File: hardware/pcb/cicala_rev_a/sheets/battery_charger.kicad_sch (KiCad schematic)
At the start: 34 parts, among them J1 USB-C receptacle, J3 Protected LiPo + NTC, U2 BQ25185DLH, U3 TPS63802DLA, U4 USBLC6-2SC6, U5 TPS22917DBVR

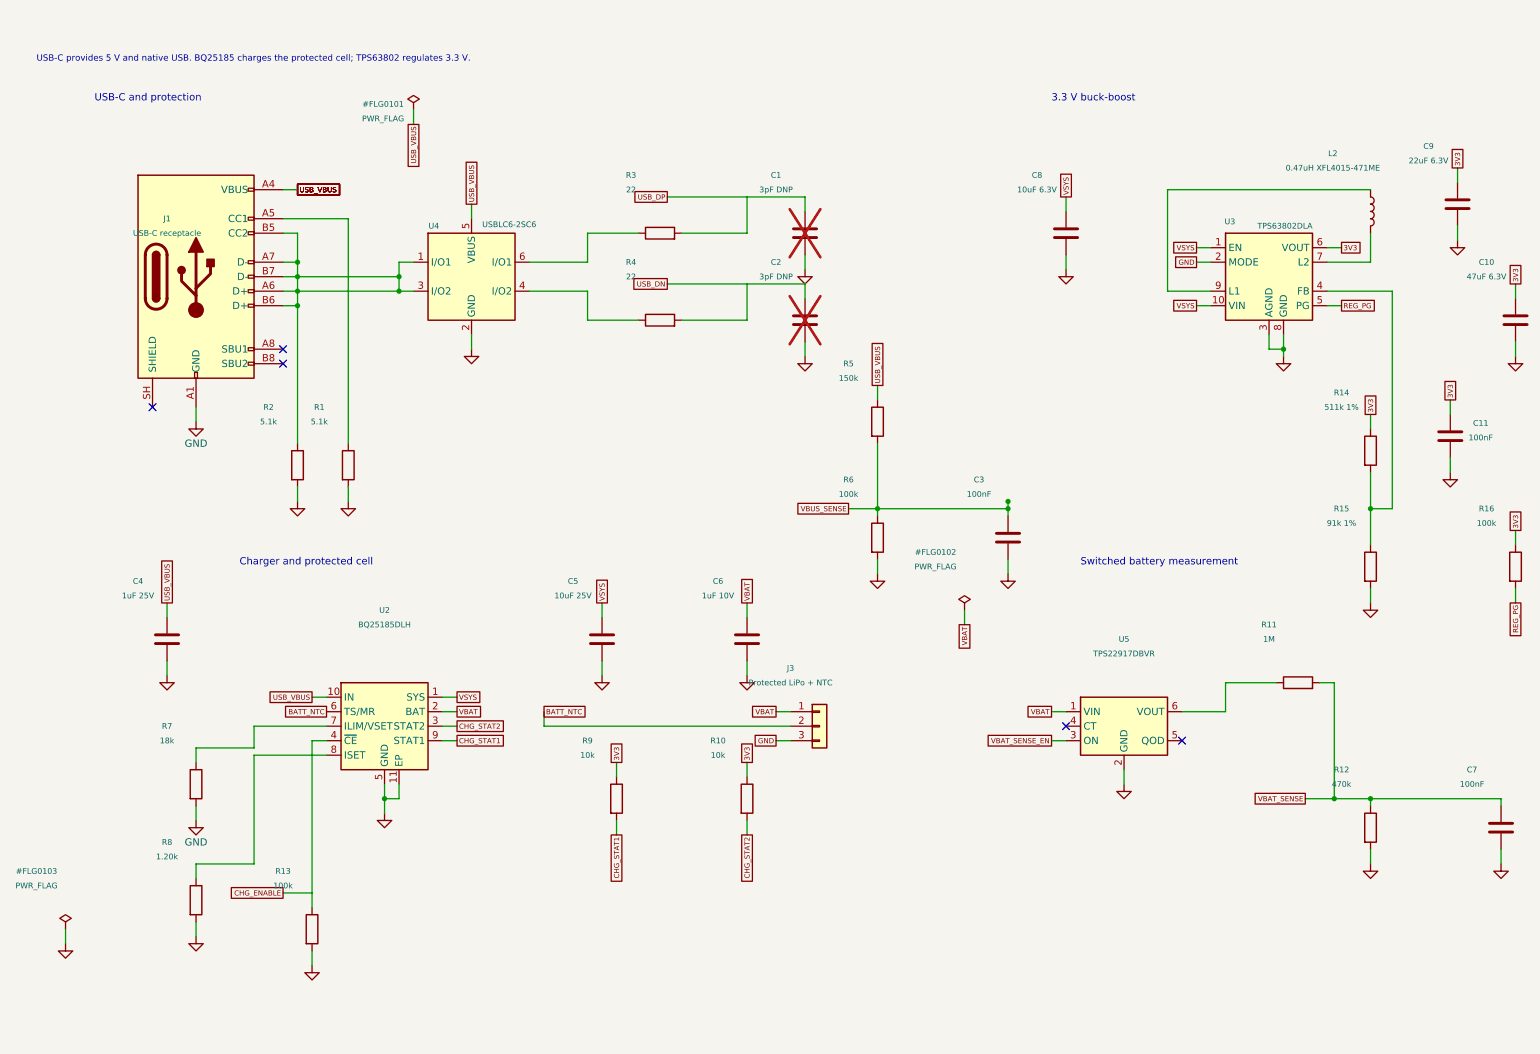
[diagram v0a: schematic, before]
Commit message: fix(hw): split the shorted USB pair and PREVGL pump node
Sheet re-layout that also separates two nets that were tied together.

J1 CC2, D+ and D- shared one net with both USBLC6 line pins; D+ and D-
are now their own nets. D1 had both pins on EPD_PREVGL, shorting it out
of the charge pump; its cathode is now the pump node with C16.

Three net labels were lost in the move and are now auto-named:
BATT_NTC, BTN_CATEGORY and BTN_NEXT. pin_contract.csv and BOM.md still
name them, so they need restoring.

Co-Authored-By: Claude Opus 5 (1M context) <noreply@anthropic.com>
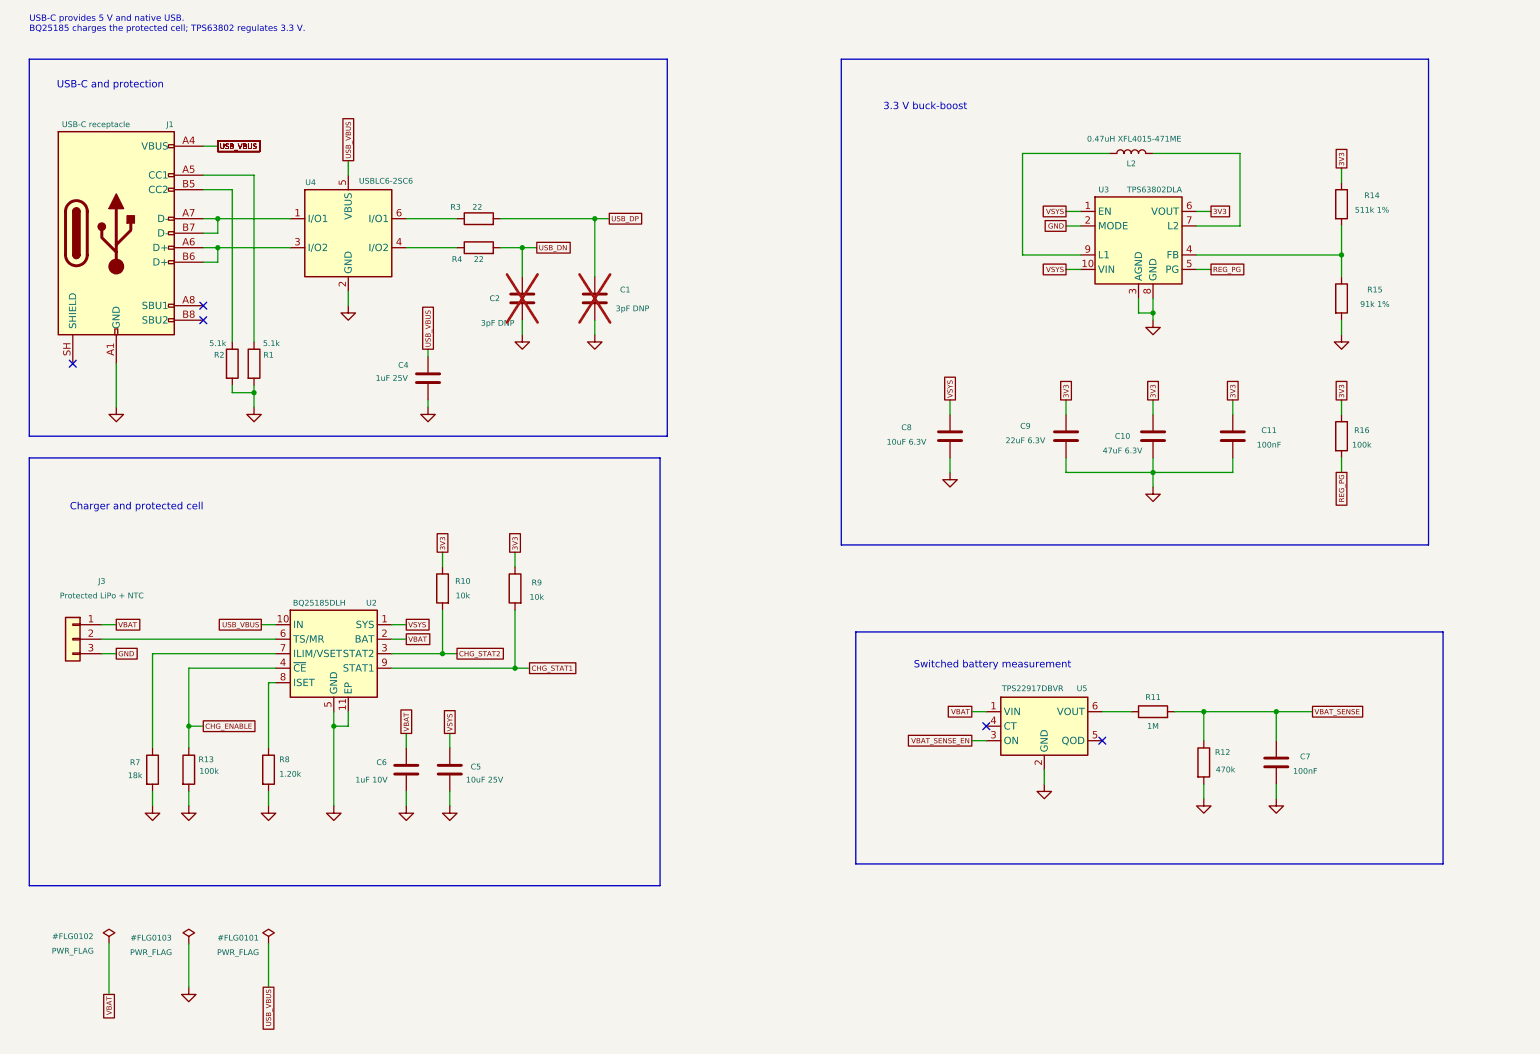
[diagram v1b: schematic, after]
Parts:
- removed C3: 100nF, Capacitor_SMD:C_0603_1608Metric, symbol Device:C
- removed R5: 150k, Resistor_SMD:R_0603_1608Metric, symbol Device:R
- removed R6: 100k, Resistor_SMD:R_0603_1608Metric, symbol Device:R
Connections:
- net BATT_NTC: no longer names the net of J3.2 (Pin_2), U2.6 (TS/MR)
- new net: J1.A6 (D+), J1.B6 (D+), U4.3 (I/O2)
- new net: J1.A7 (D-), J1.B7 (D-), U4.1 (I/O1)
- new net: J1.B5 (CC2), R2.1
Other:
- moved on the sheet: C1, C10, C11, C2, C4, C5, C6, C7, C8, C9, J1, J3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

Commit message: fix(hw): correct four ERC-invisible rev A wiring errors
All four are electrically valid connections that are simply wrong, which
is why ERC accepted them. Verified against the part datasheets and the
GDEY0213B74 reference circuit, and checked by re-exporting the netlist.

USB D+/D- were crossed between the receptacle and the MCU: J1 D- reached
GPIO20 (USB_D+) through U4 I/O1 and R3. Swapping the USB_DP and USB_DN
labels puts each line on its own pin without crossing wires. R3 now
carries D-, R4 carries D+.

Q1 used Q_NMOS_SGD, but the Si1308EDL in SOT-323 is pin 1 = G, 2 = S,
3 = D, so the gate driver landed on the sense node. The symbol is now
Q_NMOS_GSD; the drawing is unchanged because both symbols share the same
pin geometry.

D2's anode sat on EPD_PREVGL rather than on the pump node, leaving C16
with no charging path, so the negative rail could never develop. D1's
cathode, D2's anode and C16 now meet on EPD_PUMP, with D1 branching off
to EPD_PREVGL, as in the panel reference circuit.

C21 was 1 nF on VSH1, a driving rail the reference gives 1 uF/25 V.

Also restores three net names lost in the sheet re-layout: BATT_NTC,
BTN_CATEGORY and BTN_NEXT.

Co-Authored-By: Claude Opus 5 (1M context) <noreply@anthropic.com>
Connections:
- net USB_DN: now also C1.1, R3.2; no longer C2.1, R4.2
- net USB_DP: now also C2.1, R4.2; no longer C1.1, R3.2
- net BATT_NTC: now reaches J3.2 (Pin_2), U2.6 (TS/MR)

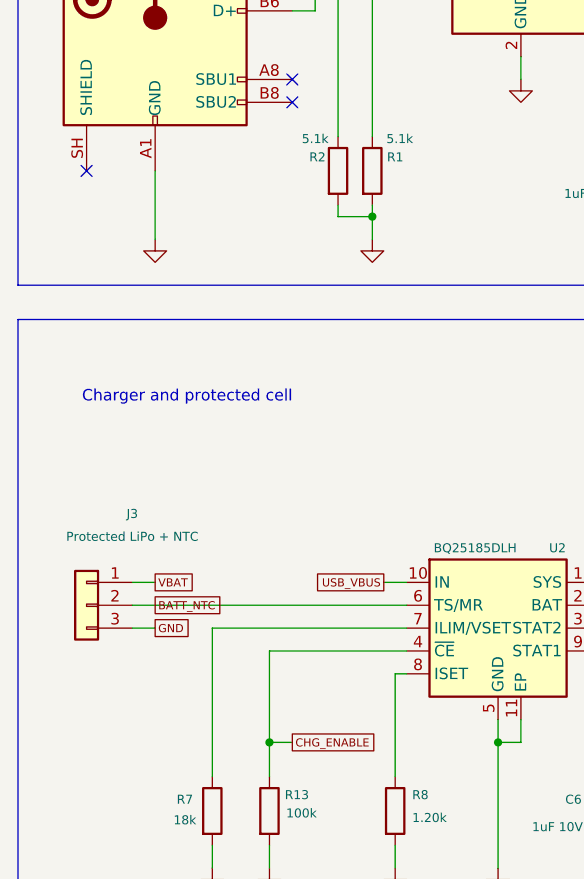
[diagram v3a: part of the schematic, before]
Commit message: feat(hw): isolate the panel bus and ground the USB-C shell
The panel's logic pins could back-power an unpowered panel through its own
ESD diodes whenever firmware deasserted EPD_PWR_EN with an output still
driven. R27-R31 put 470 ohm in series with every MCU-driven panel line, which
caps the injected current at about 5.7 mA per pin against a 3.3 V output and
a diode drop. At 4 MHz into roughly 20 pF of connector and trace the added
rise time is about 21 ns, so the same parts double as the series-tuning
positions the review asked for; fit 0 ohm to remove them during bring-up.

R32 holds the panel in reset while EPD_3V3 is off and while the MCU pin is
high-impedance. 1 M draws 3.3 uA, and only when RESET is high, which happens
only with the panel already powered.

The nets either side of the resistors are named apart: EPD_* stays the GPIO
net that pin_contract.csv and the firmware refer to, PNL_* is the panel side.

The USB-C shell had a no-connect flag and no recorded rationale. The
enclosure is plastic and carries no chassis ground, so the shell's only
discharge path is to the board. R33 (0 ohm, fitted) makes that path direct;
C31 is the alternative for a DC-isolated shell.

Co-Authored-By: Claude Opus 5 <noreply@anthropic.com>
Claude-Session: https://claude.ai/code/session_01E5vy1HJsPztSk9nFw6j5Ko
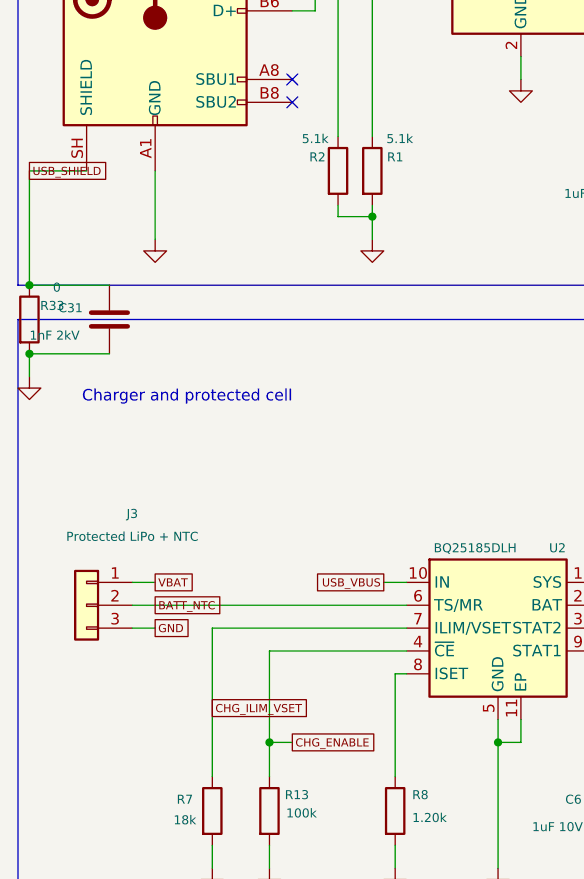
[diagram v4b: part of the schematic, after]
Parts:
- added C31: 1nF 2kV, Capacitor_SMD:C_0805_2012Metric, symbol Device:C
- added R33: 0, Resistor_SMD:R_0603_1608Metric, symbol Device:R
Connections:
- net GND: now also C31.2, R33.2
- net CHG_ILIM_VSET: now reaches R7.1, U2.7 (ILIM/VSET)
- net USB_SHIELD: now reaches J1.SH (SHIELD)
- net USB_SHIELD: now also C31.1, R33.1
- no-connect marks 5 -> 4

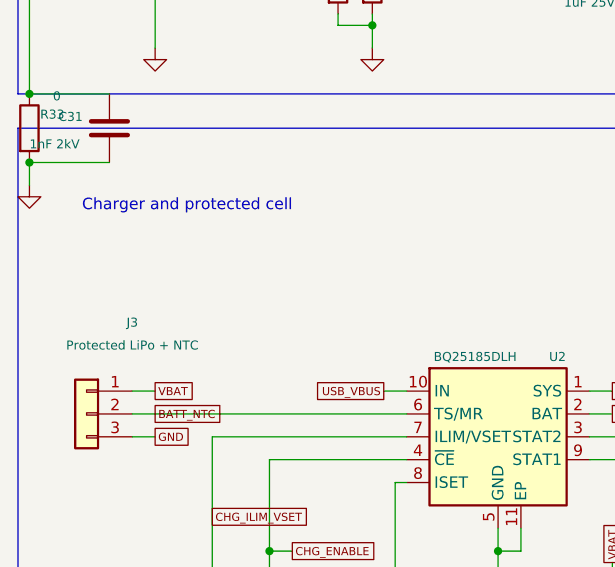
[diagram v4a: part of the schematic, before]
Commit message: feat(hw): add the production test contract and a cell-current link
TP12-TP15 expose the USB pair and both charger status lines. TP16-TP21 expose
the panel side of the display bus, next to the isolation resistors that now
live on the panel sheet where the interface they protect is drawn.

R34 is a removable 0 ohm link in the cell lead, with TP22 on the pack side.
Lifting it puts a meter between the pack and everything else, which is the
only way to measure whole-device sleep current against the 30 uA target
without cutting a trace. No link is placed in a switching loop: VSYS and 3V3
stay unbroken and are probed at TP7 and TP9.

Co-Authored-By: Claude Opus 5 <noreply@anthropic.com>
Claude-Session: https://claude.ai/code/session_01E5vy1HJsPztSk9nFw6j5Ko
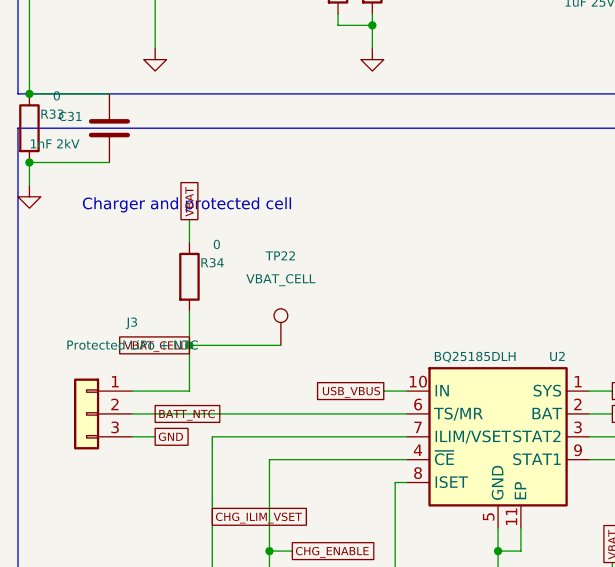
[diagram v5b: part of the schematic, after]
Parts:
- added R34: 0, Resistor_SMD:R_0603_1608Metric, symbol Device:R
- added TP22: VBAT_CELL, TestPoint:TestPoint_Pad_D1.0mm, symbol Connector:TestPoint
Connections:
- net VBAT: now also R34.1; no longer J3.1 (Pin_1)
- new net VBAT_CELL: J3.1 (Pin_1), R34.2, TP22.1
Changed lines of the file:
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@@
 	(wire
 		(pts
-			(xy 26.67 121.92) (xy 29.21 121.92)
-		)
-		(stroke
-			(width 0)
-			(type default)
-		)
-	)
-	(wire
-		(pts
 			(xy 210.82 85.09) (xy 210.82 82.55)
 		)
@@
 		)
 	)
-	(global_label "VBAT"
-		(shape passive)
-		(at 29.21 121.92 0)
-		(fields_autoplaced yes)
-		(effects
-			(font
-				(size 0.9 0.9)
-			)
-			(justify left)
-		)
-		(property "Intersheetrefs" "${INTERSHEET_REFS}"
-			(at 29.21 121.92 0)
-			(hide yes)
-			(show_name no)
-			(do_not_autoplace no)
-			(effects
-				(font
-					(size 0.8 0.8)
-				)
-			)
-		)
-	)
 	(global_label "BATT_NTC"
 		(shape passive)
@@
 				)
 			)
+		)
+	)
+	(wire
+		(pts
+			(xy 26.67 121.92) (xy 33.02 121.92)
+		)
+		(stroke
+			(width 0)
+			(type default)
+		)
+	)
+	(wire
+		(pts
+			(xy 33.02 121.92) (xy 33.02 116.84)
+		)
+		(stroke
+			(width 0)
+			(type default)
+		)
+	)
+	(wire
+		(pts
+			(xy 33.02 116.84) (xy 33.02 113.03)
+		)
+		(stroke
+			(width 0)
+			(type default)
+		)
+	)
+	(junction
+		(at 33.02 116.84)
+		(diameter 0)
+		(color 0 0 0 0)
+	)
+	(global_label "VBAT_CELL"
+		(shape passive)
+		(at 33.02 116.84 180)
+		(fields_autoplaced yes)
+		(effects
+			(font
+				(size 0.9 0.9)
+			)
+			(justify right)
+		)
+		(property "Intersheetrefs" "${INTERSHEET_REFS}"
+			(at 33.02 116.84 0)
+			(hide yes)
+			(show_name no)
+			(do_not_autoplace no)
+			(effects
+				(font
+					(size 0.8 0.8)
+				)
+			)
+		)
+	)
+	(symbol
+		(lib_id "Device:R")
+		(at 33.02 109.22 0)
+		(unit 1)
+		(body_style 1)
+		(exclude_from_sim no)
+		(in_bom yes)
+		(on_board yes)
+		(in_pos_files yes)
+		(dnp no)
+		(property "Reference" "R34"
+			(at 35.56 107.696 0)
+			(show_name no)
+			(do_not_autoplace no)
+			(effects
+				(font
+					(size 1 1)
+				)
+			)
+		)
+		(property "Value" "0"
+			(at 36.068 105.664 0)
+			(show_name no)
+			(do_not_autoplace no)
+			(effects
+				(font
+					(size 1 1)
+				)
+			)
+		)
+		(property "Footprint" "Resistor_SMD:R_0603_1608Metric"
+			(at 33.02 109.22 0)
+			(hide yes)
+			(show_name no)
+			(do_not_autoplace no)
+			(effects
+				(font
+					(size 1 1)
+				)
+			)
+		)
+		(property "Datasheet" "~"
+			(at 33.02 109.22 0)
+			(hide yes)
+			(show_name no)
+			(do_not_autoplace no)
+			(effects
+				(font
+					(size 1 1)
+				)
+			)
+		)
+		(property "Description" "Resistor"
+			(at 33.02 109.22 0)
+			(hide yes)
+			(show_name no)
+			(do_not_autoplace no)
+			(effects
+				(font
+					(size 1 1)
+				)
+			)
+		)
+		(pin "1"
+		)
+		(pin "2"
+		)
+		(instances
+			(project "cicala_rev_a"
+				(path "/9b5e4c31-c66f-4b64-9ff8-62a2c447d0bc/76abdd1f-1863-43cb-987e-b8bd556e1e12"
+					(reference "R34")
+					(unit 1)
+				)
+			)
+		)
+	)
+	(wire
+		(pts
+			(xy 33.02 105.41) (xy 33.02 102.87)
+		)
+		(stroke
+			(width 0)
+			(type default)
+		)
+	)
+	(global_label "VBAT"
+		(shape passive)
+		(at 33.02 102.87 90)
+		(fields_autoplaced yes)
+		(effects
+			(font
+				(size 0.9 0.9)
+			)
+			(justify left)
+		)
+		(property "Intersheetrefs" "${INTERSHEET_REFS}"
+			(at 33.02 102.87 0)
+			(hide yes)
+			(show_name no)
+			(do_not_autoplace no)
+			(effects
+				(font
+					(size 0.8 0.8)
+				)
+			)
+		)
+	)
+	(wire
+		(pts
+			(xy 33.02 116.84) (xy 43.18 116.84)
+		)
+		(stroke
+			(width 0)
+			(type default)
+		)
+	)
+	(symbol
+		(lib_id "Connector:TestPoint")
+		(at 43.18 116.84 0)
+		(unit 1)
+		(body_style 1)
+		(exclude_from_sim no)
+		(in_bom no)
+		(on_board yes)
+		(in_pos_files yes)
+		(dnp no)
+		(property "Reference" "TP22"
+			(at 43.18 106.934 0)
+			(show_name no)
+			(do_not_autoplace no)
+			(effects
+				(font
+					(size 1 1)
+				)
+			)
+		)
+		(property "Value" "VBAT_CELL"
+			(at 43.18 109.474 0)
+			(show_name no)
+			(do_not_autoplace no)
+			(effects
+				(font
+					(size 1 1)
+				)
+			)
+		)
+		(property "Footprint" "TestPoint:TestPoint_Pad_D1.0mm"
+			(at 43.18 116.84 0)
+			(hide yes)
+			(show_name no)
+			(do_not_autoplace no)
+			(effects
+				(font
+					(size 1 1)
+				)
+			)
+		)
+		(property "Datasheet" "~"
+			(at 43.18 116.84 0)
+			(hide yes)
+			(show_name no)
+			(do_not_autoplace no)
+			(effects
+				(font
+					(size 1 1)
+				)
+			)
+		)
+		(property "Description" "test point"
+			(at 43.18 116.84 0)
+			(hide yes)
+			(show_name no)
+			(do_not_autoplace no)
+			(effects
+				(font
+					(size 1 1)
+				)
+			)
+		)
+		(pin "1"
+		)
+		(instances
+			(project "cicala_rev_a"
+				(path "/9b5e4c31-c66f-4b64-9ff8-62a2c447d0bc/5c37343c-ce2e-4af1-8c0e-7996e7e59814"
+					(reference "TP22")
+					(unit 1)
+				)
+			)
